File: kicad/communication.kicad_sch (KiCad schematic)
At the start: 35 parts, among them J3 CAN0A, J4 CAN0B, J6 CAN1A, J7 CAN1B, U12 TJA1462ATK, U13 TJA1462ATK, U14 SK9822-EC20

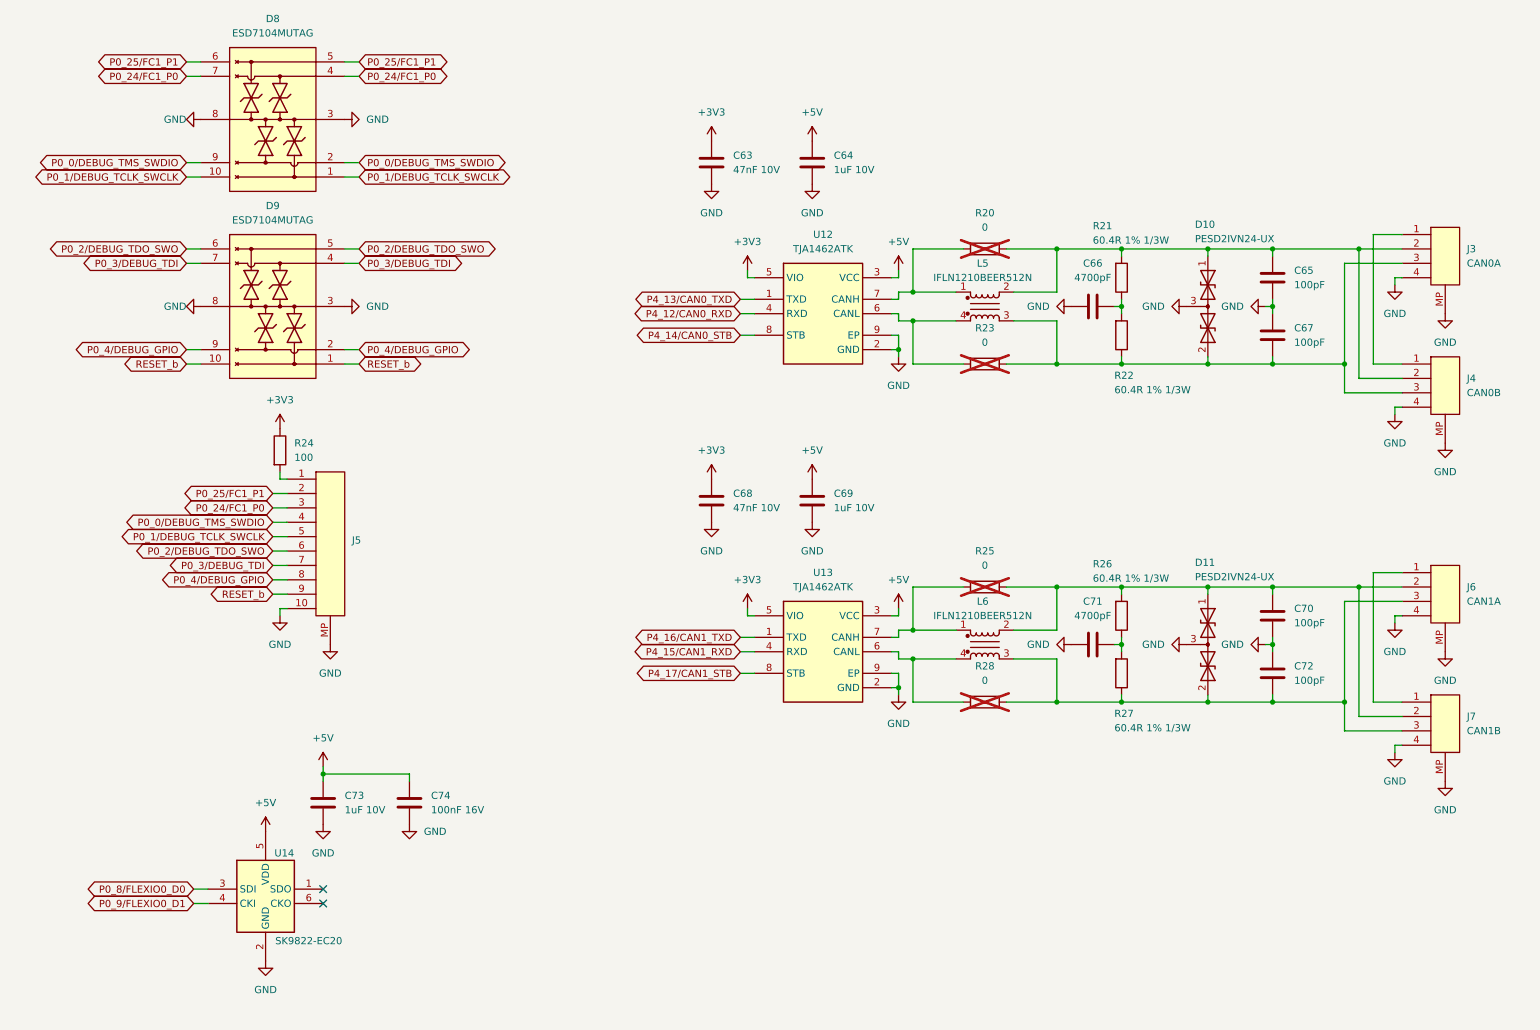
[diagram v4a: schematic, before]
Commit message: Updated schematic after feedback from Jari
- Finished schematic after feedback from Jari. It is at a finished state, can be reviewed by whole team now.
- Layouted MCXN with decoupling caps.
- Layouted Base100-T1 ethernet phy.
- Layouted the power supply a bit.
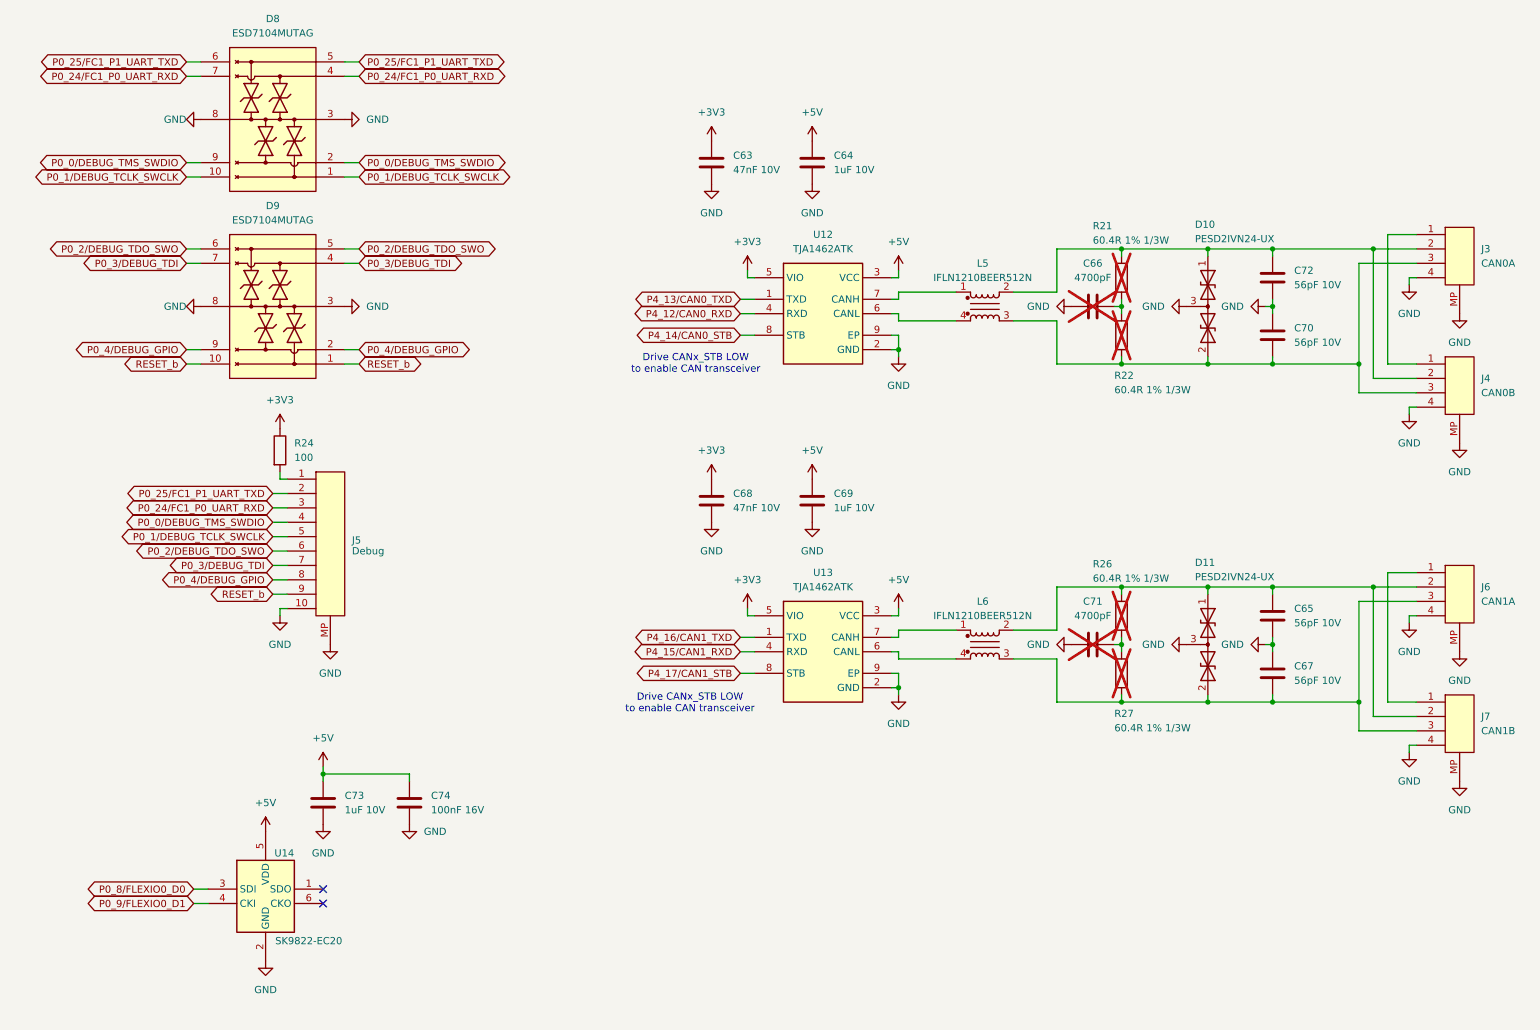
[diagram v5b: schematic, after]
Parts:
- removed R20, R23, R25, R28: 0, Resistor_SMD:R_0402_1005Metric, symbol Device:R
- C65, C67, C70, C72: value 100pF -> 56pF 10V; footprint Capacitor_SMD:C_0402_1005Metric -> (none); MF YAGEO -> (none); MFPN CC0402JRNPO9BN101 -> (none); Supplier JLCPCB -> (none); Supplier PN C106200 -> (none)
- C66, C71, R21, R22, R26, R27: now not fitted
- J3, J4, J6, J7: MF (none) -> JST; MFPN (none) -> SM04B-GHS-TB(LF)(SN); Supplier (none) -> JLCPCB; Supplier PN (none) -> C189895
- J5: value ~ -> Debug; MF (none) -> JST; MFPN (none) -> SM10B-SRSS-TB(LF)(SN); Supplier (none) -> JLCPCB; Supplier PN (none) -> C160409
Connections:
- net GND: now also C65.2, C67.1; no longer C65.1, C67.2
- net at D11.1 (A1), J6.2 (1), J7.2 (1)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: now also C65.1; no longer C70.2
- net at D10.2 (A2), J3.3 (1), J4.3 (1)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: now also C70.2; no longer C67.1
- net at D10.1 (A1), J3.2 (1), J4.2 (1)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: now also C72.1; no longer C65.2
- net at D11.2 (A2), J6.3 (1), J7.3 (1)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: now also C67.2; no longer C72.1
- net P0_24/FC1_P0 renamed P0_24/FC1_P0_UART_RXD
- net P0_25/FC1_P1 renamed P0_25/FC1_P1_UART_TXD
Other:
- note added: "Drive CANx_STB LOW to enable CAN transceiver"
- title: MR-MCXN-T1 Sensor hub -> MR-MCXN-T1 Sensor Node
- moved on the sheet: J3, J4, J6, J7

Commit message: Finished schematic. Completed power and ENET phy layout.
Layouted power supply and ethernet phy around input connector.
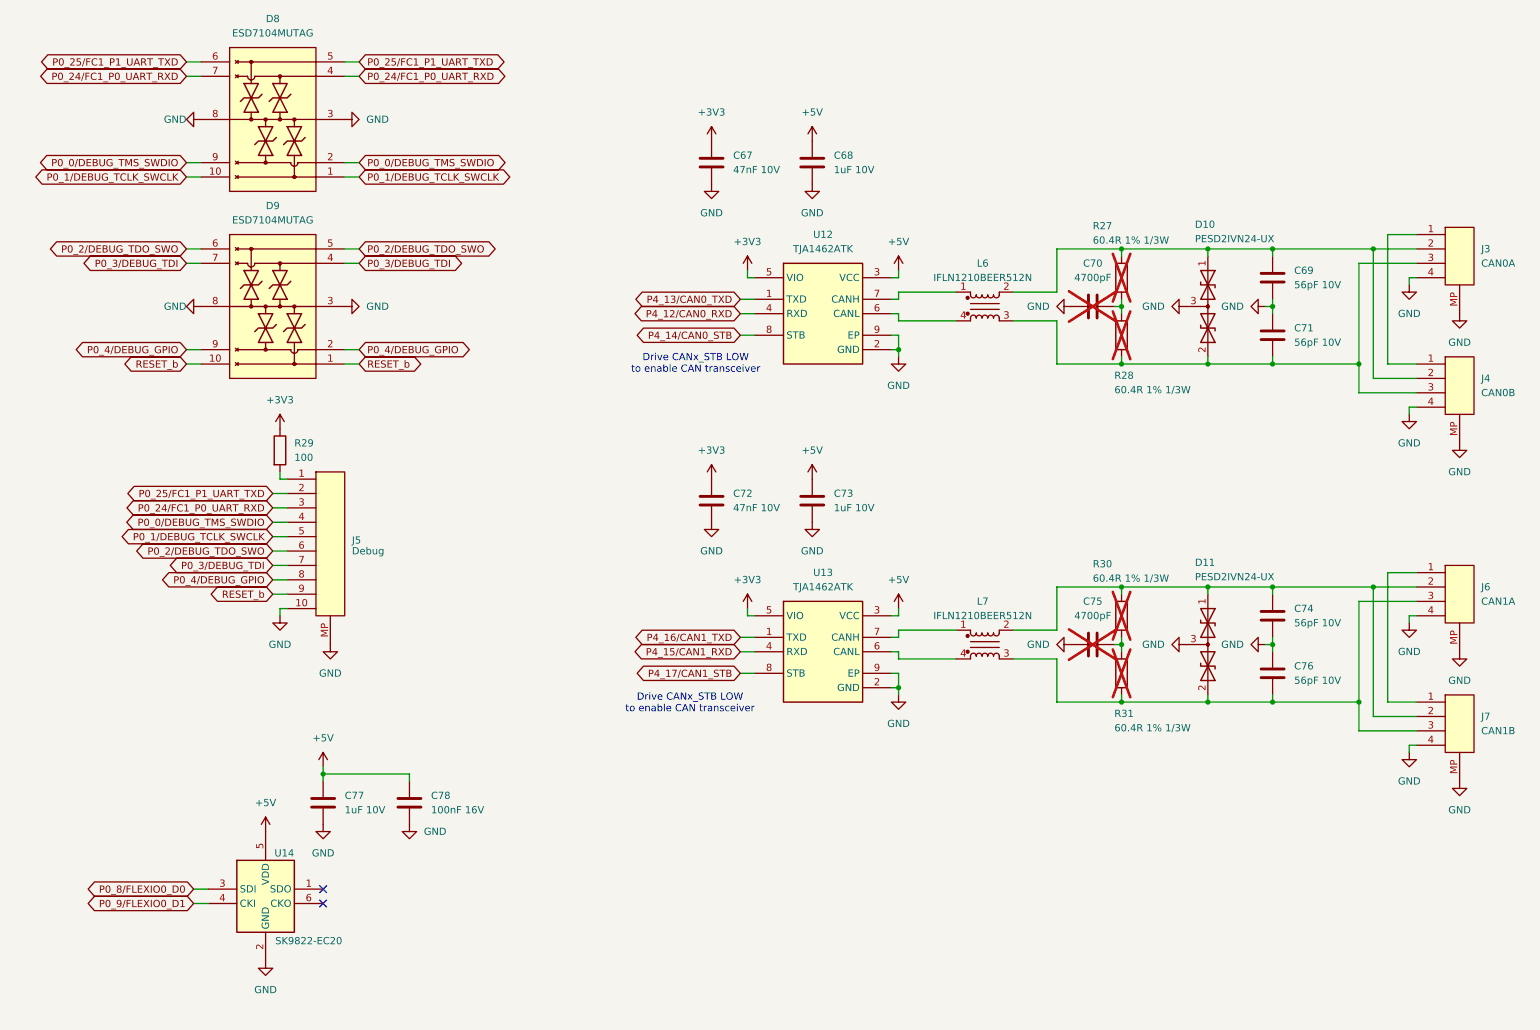
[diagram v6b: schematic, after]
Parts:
- C68: renamed from C64; footprint Capacitor_SMD:C_0603_1608Metric -> Capacitor_SMD:C_0402_1005Metric; MF Samsung Electro-Mechanics -> Murata Electronics; MFPN CL10B105KA8NNNC -> GRM155Z71A105KE01D; Supplier PN C29936 -> C528974
- C69: renamed from C72; footprint (none) -> Capacitor_SMD:C_0402_1005Metric; MF (none) -> YAGEO; MFPN (none) -> CC0402JRNPO9BN560; Supplier (none) -> JLCPCB; Supplier PN (none) -> C107007
- C71: renamed from C70; footprint (none) -> Capacitor_SMD:C_0402_1005Metric; MF (none) -> YAGEO; MFPN (none) -> CC0402JRNPO9BN560; Supplier (none) -> JLCPCB; Supplier PN (none) -> C107007
- C73: renamed from C69; footprint Capacitor_SMD:C_0603_1608Metric -> Capacitor_SMD:C_0402_1005Metric; MF Samsung Electro-Mechanics -> Murata Electronics; MFPN CL10B105KA8NNNC -> GRM155Z71A105KE01D; Supplier PN C29936 -> C528974
- C74: renamed from C65; footprint (none) -> Capacitor_SMD:C_0402_1005Metric; MF (none) -> YAGEO; MFPN (none) -> CC0402JRNPO9BN560; Supplier (none) -> JLCPCB; Supplier PN (none) -> C107007
- C76: renamed from C67; footprint (none) -> Capacitor_SMD:C_0402_1005Metric; MF (none) -> YAGEO; MFPN (none) -> CC0402JRNPO9BN560; Supplier (none) -> JLCPCB; Supplier PN (none) -> C107007
- C77: renamed from C73; footprint Capacitor_SMD:C_0603_1608Metric -> Capacitor_SMD:C_0402_1005Metric; MF Samsung Electro-Mechanics -> Murata Electronics; MFPN CL10B105KA8NNNC -> GRM155Z71A105KE01D; Supplier PN C29936 -> C528974
- renumbered C63 to C67, C66 to C70, C68 to C72, C71 to C75, C74 to C78, L5 to L6, L6 to L7, R21 to R27, R22 to R28, R24 to R29, R26 to R30, R27 to R31

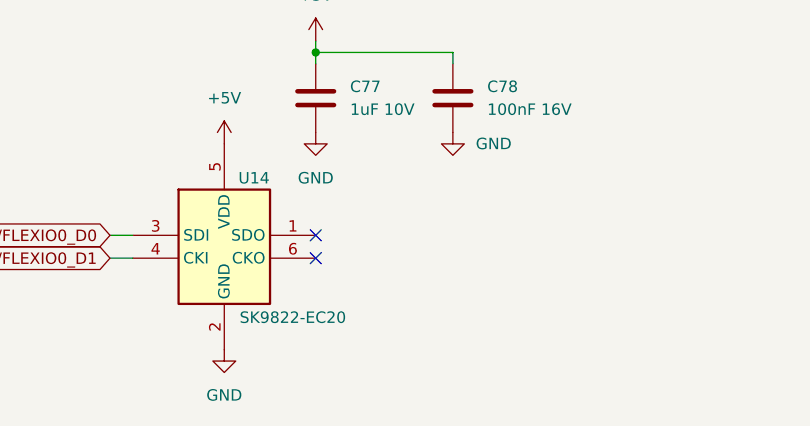
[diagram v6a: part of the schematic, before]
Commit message: Updated PCB layout
Implemented feedback:
- Placed ENET LEDs next to each other
- Added solder pads to output of RGB LED
- Made hole to hole distance in X-axis to 30.5mm
- Placed IMU a bit closer to the middle to still comply to the design rules by TDK.
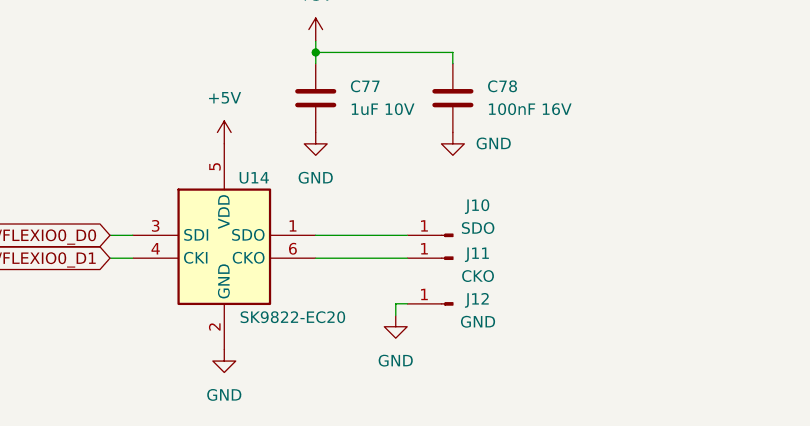
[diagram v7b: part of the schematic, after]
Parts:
- added J10: SDO, Connector_Wire:SolderWirePad_1x01_SMD_1x2mm, symbol Connector:Conn_01x01_Pin
- added J11: CKO, Connector_Wire:SolderWirePad_1x01_SMD_1x2mm, symbol Connector:Conn_01x01_Pin
- added J12: GND, Connector_Wire:SolderWirePad_1x01_SMD_1x2mm, symbol Connector:Conn_01x01_Pin
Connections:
- net GND: now also J12.1 (Pin_1)
- net at U14.1 (SDO): now also J10.1 (Pin_1)
- net at U14.6 (CKO): now also J11.1 (Pin_1)
- no-connect marks 2 -> 0

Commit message: Updated layout and BOM
- Rounded corners of PCB
- Updated board-to-board MFPN to correct one.
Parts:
- J10, J11, J12: now left out of the parts list
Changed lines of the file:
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@@
 		(unit 1)
 		(exclude_from_sim no)
-		(in_bom yes)
+		(in_bom no)
 		(on_board yes)
 		(dnp no)
@@
 		(unit 1)
 		(exclude_from_sim no)
-		(in_bom yes)
+		(in_bom no)
 		(on_board yes)
 		(dnp no)
@@
 		(unit 1)
 		(exclude_from_sim no)
-		(in_bom yes)
+		(in_bom no)
 		(on_board yes)
 		(dnp no)
